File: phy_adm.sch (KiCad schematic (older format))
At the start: 29 parts

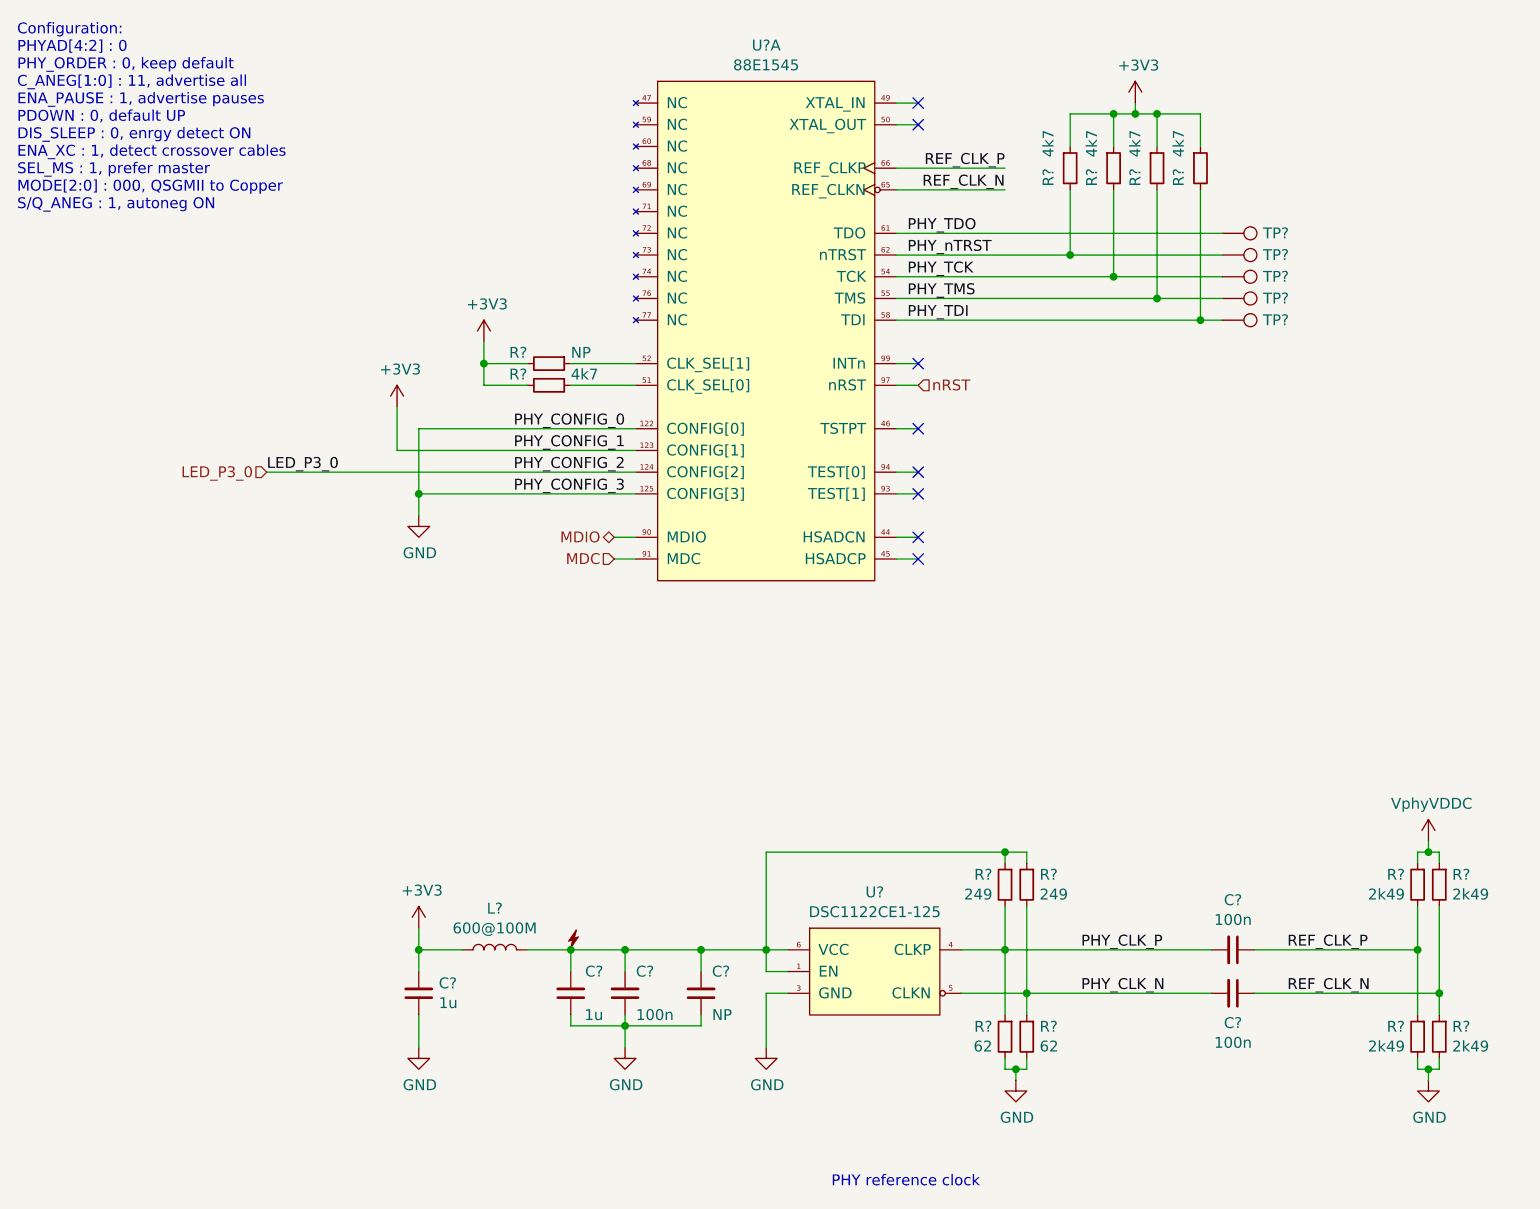
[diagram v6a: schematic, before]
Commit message: sch: Annotate & associate symbols with footprints
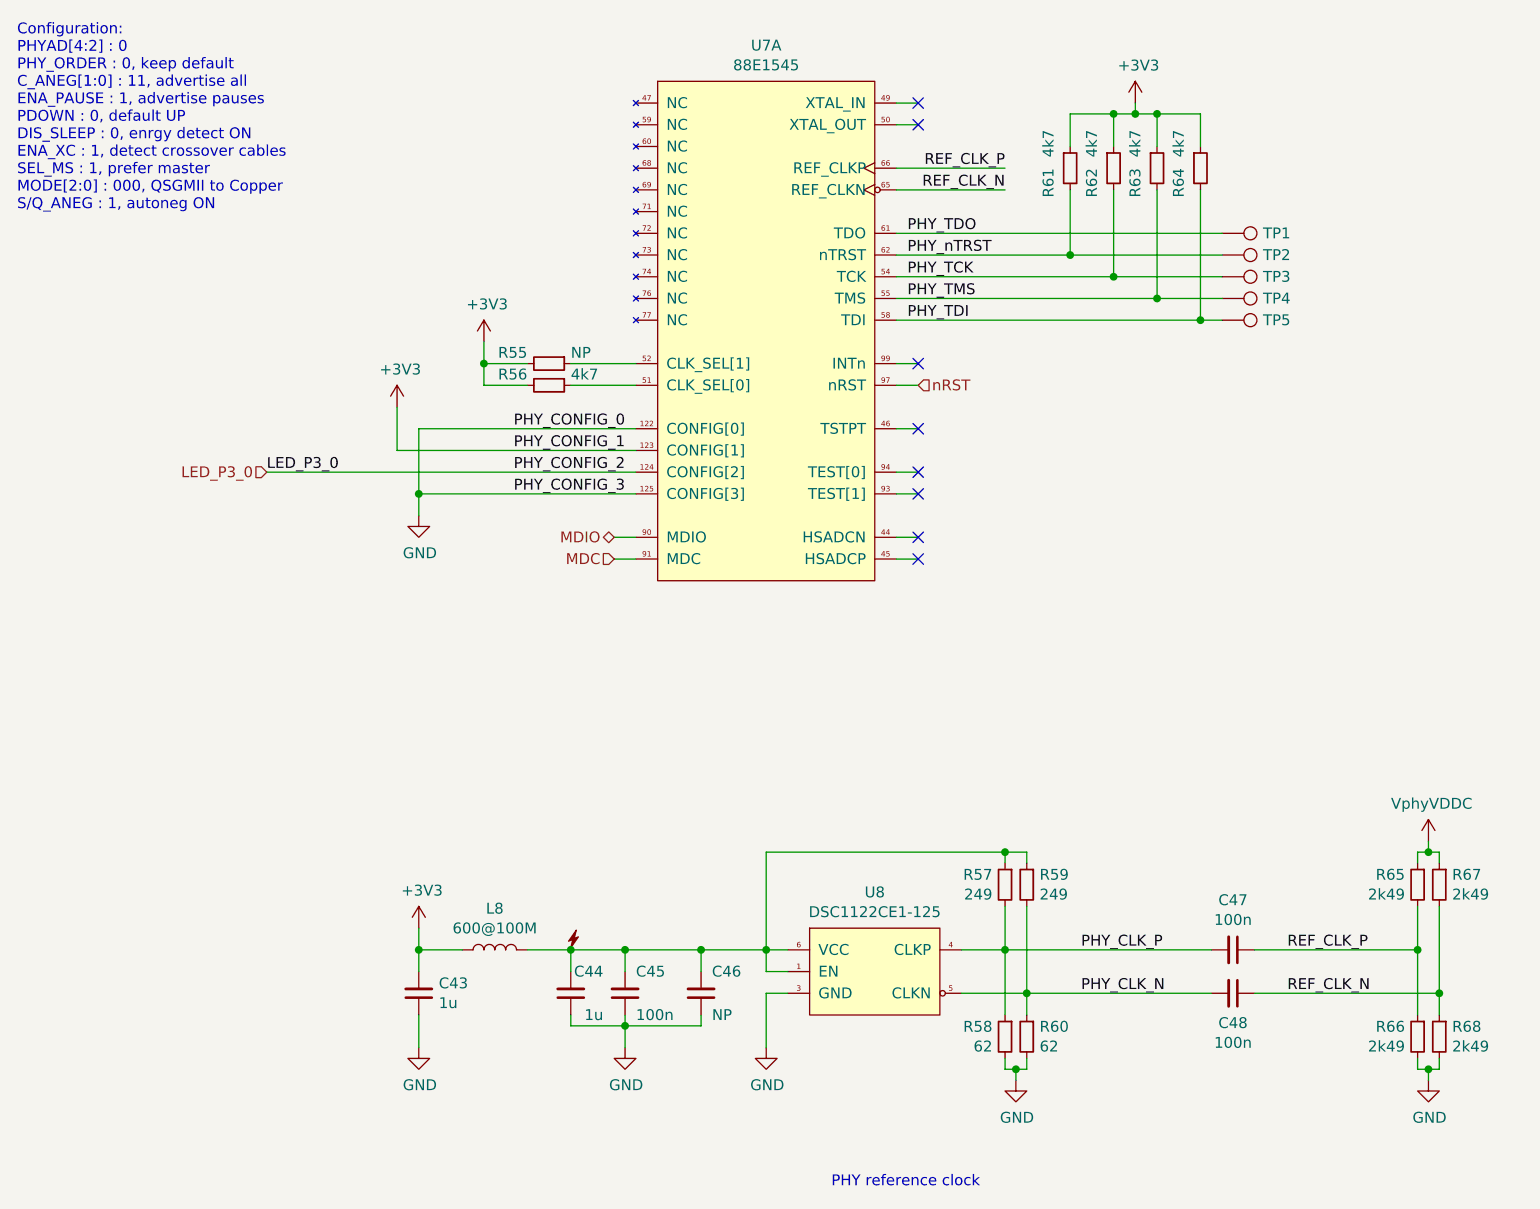
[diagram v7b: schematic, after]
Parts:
- removed DS?: DummySupply, symbol pimouss-motherboard:DummySupply
- C43, C44, C45, C46: renamed from C?; footprint (none) -> Capacitor_SMD:C_0603_1608Metric
- C47, C48: renamed from C?; footprint (none) -> Capacitor_SMD:C_0402_1005Metric
- L8: renamed from L?; footprint (none) -> Inductor_SMD:L_0603_1608Metric
- R55, R56, R61, R62, R63, R64: renamed from R?; footprint (none) -> Resistor_SMD:R_0603_1608Metric
- R57, R58, R59, R60, R65, R66, R67, R68: renamed from R?; footprint (none) -> Resistor_SMD:R_0402_1005Metric
- TP1, TP2, TP3, TP4, TP5: renamed from TP?; footprint (none) -> TestPoint:TestPoint_Pad_D1.0mm
- gave numbers to parts that had none: 2

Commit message: sch: Fix PHY ref clk footprint
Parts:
- U8: footprint Package_DFN_QFN:DFN-6_2.5x2mm_P0.825mm -> pimouss-motherboard:DFN-6_2.5x2mm_P0.825mm
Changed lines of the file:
@@
 F 0 "U8" H 5000 5365 50  0000 C CNN
 F 1 "DSC1122CE1-125" H 5000 5274 50  0000 C CNN
-F 2 "Package_DFN_QFN:DFN-6_2.5x2mm_P0.825mm" H 5650 4700 50  0001 C CNN
+F 2 "pimouss-motherboard:DFN-6_2.5x2mm_P0.825mm" H 5650 4700 50  0001 C CNN
 F 3 "http://ww1.microchip.com/downloads/en/DeviceDoc/DSC1102%20DSC1122%20Datasheet%20MKQBPD11041002-6.pdf" H 4700 5350 50  0001 C CNN
 	1    4700 5200
